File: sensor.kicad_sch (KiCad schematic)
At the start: 15 parts, among them IC1 A3909, J1 Micro_SD_Card_Det1, U2 IMU, U5 LPS22HB, U6 GPS, U7 SX1276, U8 NAND

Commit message: Changes, idr what though :(
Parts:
- removed R13: 10kΩ, symbol Device:R
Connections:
- net +3.3V: now also R12.1
- net GND: now also U7.15 (GND), U7.23 (GND), U7.26 (GND), U7.29 (GND)
- net MISO TMCU: now also U7.17 (MISO)
- net MOSI TMCU: now also U7.18 (MOSI)
- net at R12.2, U8.3 (~{WP}/IO_{2}): now also U8.7 (~{HOLD}/~{RESET}/IO_{3})
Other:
- note added: "Baro"
- note added: "Chip Selection"
- note added: "GPS"
- note added: "IMU"
- note added: "Interrupt Pin"
- note added: "RF"
- note added: "Storage/Logging"
- note added: "UART Lines"
- moved on the sheet: C14, C15, IC1, J1, R10, R12, R8, R9, U2, U5, U7, U8

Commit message: misc fixes
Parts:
- added C18: 4.7uF, symbol Device:C
- added C19: 100nF, symbol Device:C
- added D1: D_Schottky, symbol Device:D_Schottky
- added R19, R23: 10k, symbol Device:R
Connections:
- net +3.3V: now also C18.2, C19.2, D1.2 (A); no longer U6.8 (V_BCKP)
- net GND: now also C18.1, C19.1, R19.1, R23.1
- net at U7.8 (DIO0): now also R19.2
- net at U7.9 (DIO1): now also R23.2
- new net: D1.1 (K), U6.8 (V_BCKP)

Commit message: GPS is done! yay
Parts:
- added C20: 100nF, symbol Device:C
- added D2: PESD5V‑S5ULC, symbol Device:D
- added J3: Conn_Coaxial, symbol Connector:Conn_Coaxial
- added L1: 47 nH, Inductor_SMD:L_6.3x6.3_H3, symbol Device:L_Ferrite_Small
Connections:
- net +3.3V: now also L1.1
- net GND: now also D2.1 (K), J3.2 (Ext)
- net at U6.16 (RF_OUT): now also C20.2
- new net: C20.1, D2.2 (A), J3.1 (In), L1.2
- no-connect marks 7 -> 15
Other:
- note added: "Confirm L4 has ≥1 kΩ impedance at 1.575 GHz"
- note added: "No Noise within 3mm of this chain 50 Ω trace keep RF_OUT → C20 → SMA center < 5 mm"

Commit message: RF at 915MHZ done!
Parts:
- added C21: 2.2 pF, symbol Device:C
- added C22: 1.8 pF, symbol Device:C
- added J4: H9161TR-ND, symbol Connector:Conn_Coaxial_Small
- added L7: 5.6 nH, symbol Device:L
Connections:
- net GND: now also C22.1, J4.2 (Ext)
- net at U7.22 (RFO_HF): now also C21.1
- new net: C21.2, J4.1 (In), L7.1
- new net: C22.2, L7.2
- no-connect marks 15 -> 16
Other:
- note added: "No Noise within 3mm of this chain 50 Ω trace keep RF_OUT → C20 → SMA center < 6 mm"
- note added: "RF at 915MHZ"
- note removed: "RF"
- moved on the sheet: R19, R23, U7

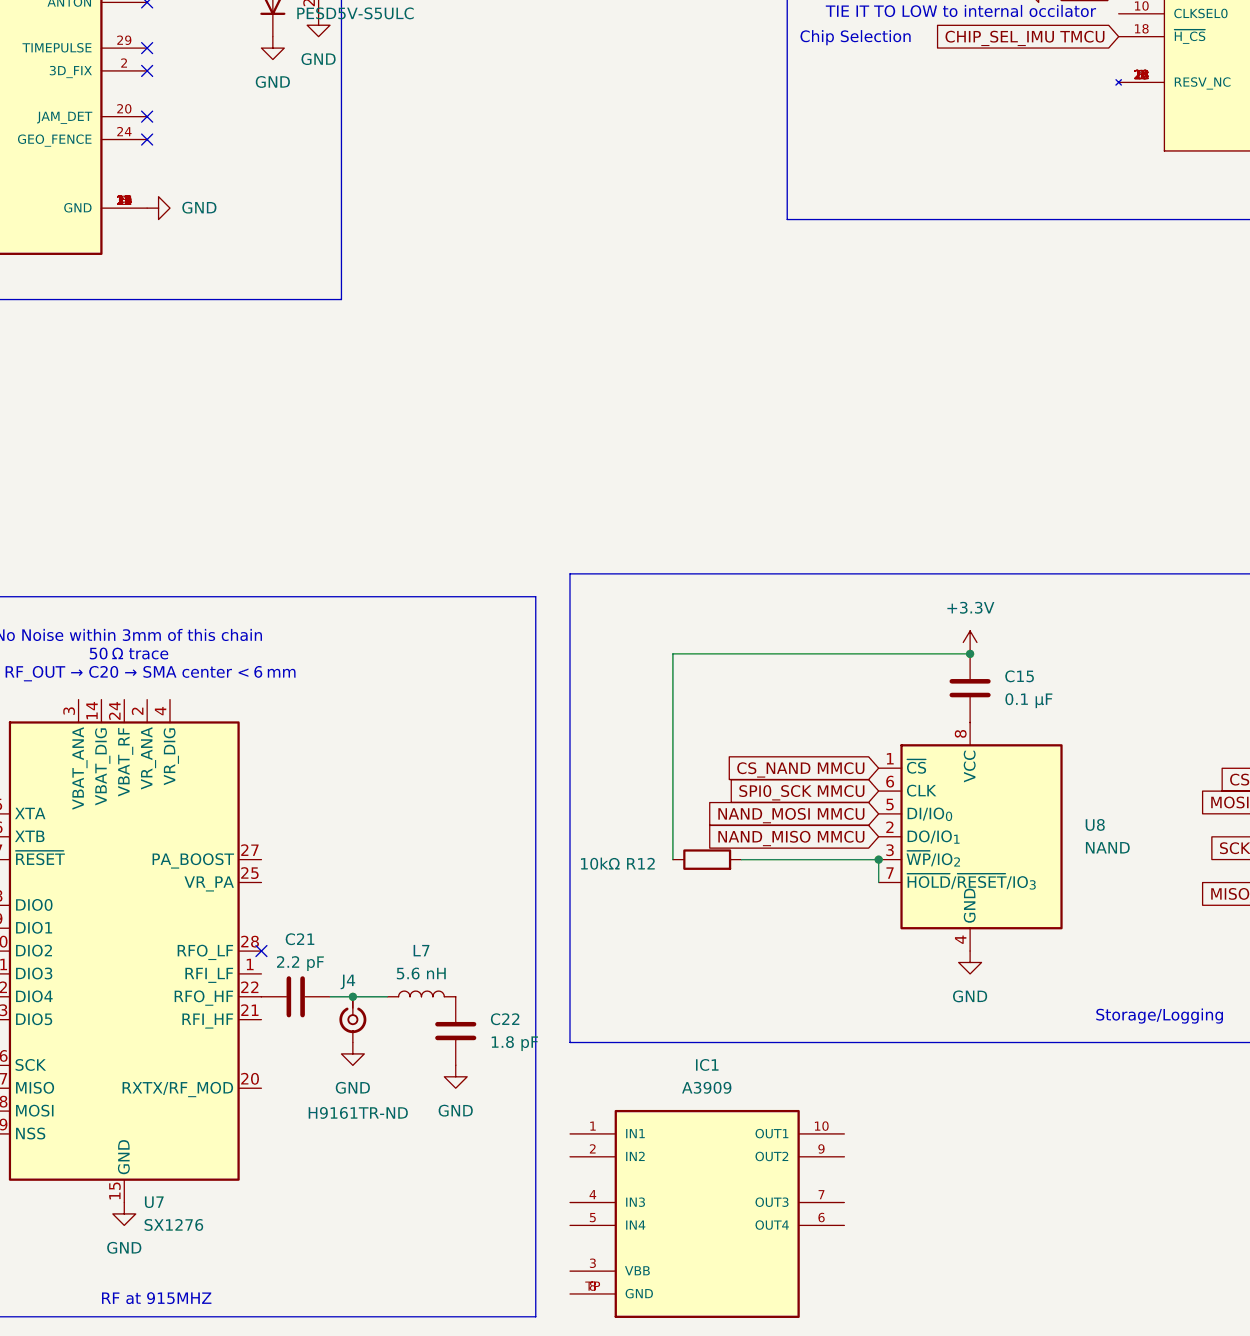
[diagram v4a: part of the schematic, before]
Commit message: H-Bridge is done!
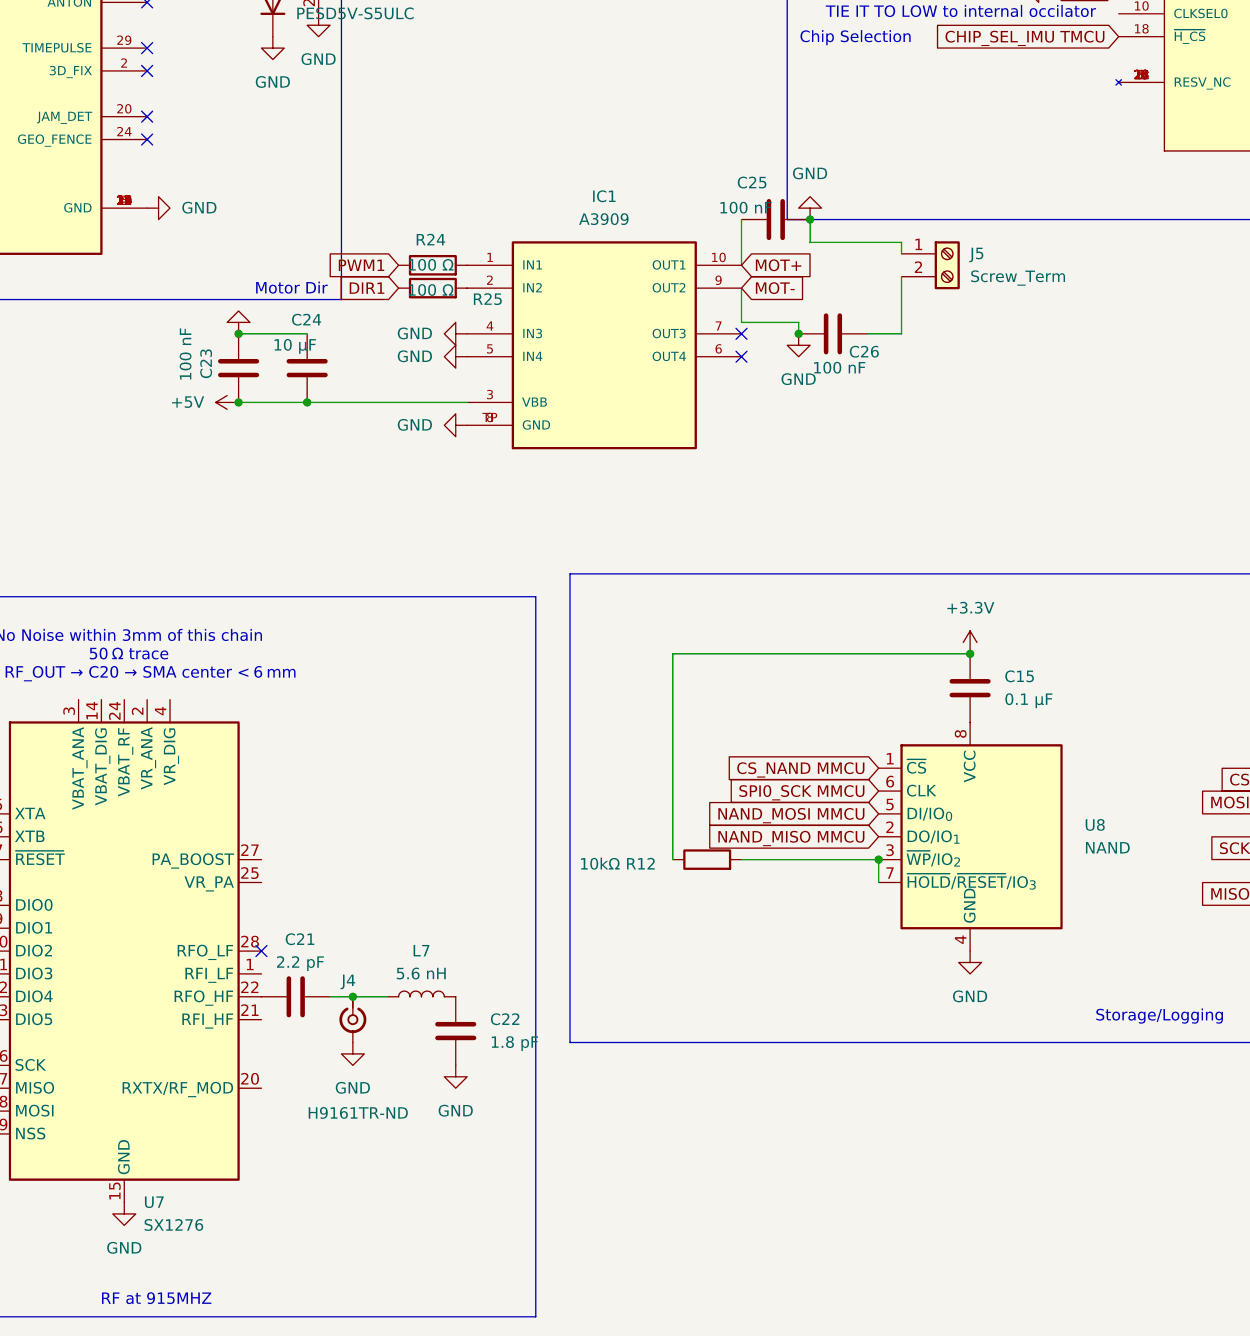
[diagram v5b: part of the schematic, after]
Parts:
- added C23, C25, C26: 100 nF, symbol Device:C
- added C24: 10 µF, symbol Device:C
- added J5: Screw_Term, symbol Connector:Screw_Terminal_01x02
- added R24, R25: 100 Ω, symbol Device:R
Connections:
- net GND: now also IC1.4 (IN3), IC1.5 (IN4), IC1.8 (GND), IC1.9 (OUT2), IC1.TP (GND), C23.1, C24.1, C25.1, C26.2, J5.1 (Pin_1)
- net at IC1.1 (IN1): now also R24.2
- net MOT+: now reaches IC1.10 (OUT1)
- net MOT+: now also C25.2
- net at IC1.2 (IN2): now also R25.2
- net +5V: now reaches IC1.3 (VBB)
- net +5V: now also C23.2, C24.2
- new net: C26.1, J5.2 (Pin_2)
- new net DIR1: R25.1
- new net PWM1: R24.1
- no-connect marks 16 -> 18
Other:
- note added: "Motor Dir"
- moved on the sheet: IC1

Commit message: Flag Changes- Important
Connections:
- net MISO_SD MMCU is gone; now on net NAND_MISO MMCU: J1.7 (DAT0)
- net MOSI_SD MMCU is gone; now on net NAND_MOSI MMCU: J1.3 (CMD)
- net SCK_SD MMCU renamed SPI0_SCK MMCU
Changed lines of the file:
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@@
 		)
 	)
-	(global_label "MOSI_SD MMCU"
+	(global_label "NAND_MOSI MMCU"
 		(shape input)
 		(at 227.33 138.43 180)
@@
 		)
 		(property "Intersheetrefs" "${INTERSHEET_REFS}"
-			(at 209.8306 138.43 0)
+			(at 207.2905 138.43 0)
 			(effects
 				(font
@@
 		)
 	)
-	(global_label "MISO_SD MMCU"
+	(global_label "NAND_MISO MMCU"
 		(shape input)
 		(at 227.33 148.59 180)
@@
 		)
 		(property "Intersheetrefs" "${INTERSHEET_REFS}"
-			(at 209.8306 148.59 0)
+			(at 207.2905 148.59 0)
 			(effects
 				(font
@@
 		)
 	)
-	(global_label "SCK_SD MMCU"
+	(global_label "SPI0_SCK MMCU"
 		(shape input)
 		(at 227.33 143.51 180)
@@
 		)
 		(property "Intersheetrefs" "${INTERSHEET_REFS}"
-			(at 210.6773 143.51 0)
-			(effects
-				(font
+			(at 208.863 143.51 0)
+			(effects
+				(font

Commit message: chip wiring fix
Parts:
- added C44, C45, C48, C49, C50, C51, C52, C53, C54, C55, C56, C57, C58: 100nF, symbol Device:C
- added C46, C47: 22pF, symbol Device:C_Polarized_US
- added J12, J13, J14, J6, J9: Conn_01x03, Connector_PinHeader_2.54mm:PinHeader_1x03_P2.54mm_Vertical, symbol Connector_Generic:Conn_01x03
- added Q1, Q3, Q4, Q5, Q6: 2N7002, Package_TO_SOT_SMD:SOT-23, symbol Transistor_FET:2N7002
- added R27, R31, R32, R33, R34, R35, R36, R37, R38, R39, R52, R53, R56, R57: 10k, symbol Device:R
- added R54, R55: 10kΩ, symbol Device:R
- added R58, R59, R60, R61, R62, R63, R64, R65, R66, R67: R, symbol Device:R
- added U10: LSM6DS3, Package_LGA:LGA-14_3x2.5mm_P0.5mm_LayoutBorder3x4y, symbol Sensor_Motion:LSM6DS3
- added Y2: 32.768kHz, symbol Device:Crystal
- C15: value 0.1 µF -> 100nF
- C24: value 10 µF -> 10nF
- C25: value 100 nF -> 100nF
- C26: value 100 nF -> 10nF
- R24, R25: value 100 Ω -> 10k
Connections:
- net +3.3V: now also U7.14 (VBAT_DIG), U7.2 (VR_ANA), U7.24 (VBAT_RF), U7.3 (VBAT_ANA), U7.4 (VR_DIG), U8.8 (VCC), C44.2, C45.2, C48.2, C49.2, C50.2, C51.2, C52.2, C53.2, C54.2, C55.2, C56.2, R27.1, R32.1, R33.1, R34.1, R35.1, R36.1, R37.1, R38.1, R39.1, R52.1, R53.1, R54.1, R55.1, R56.1, R57.1, U10.5 (VDDIO), U10.8 (VDD); no longer R11.1, R9.1
- net +5V: now also R58.1, R59.1, R60.1, R61.1, R62.1; no longer C24.2
- net CS_SD MMCU: now also R55.2
- net DIR1: now also IC1.2 (IN2), R24.2; no longer R25.1
- net GND: now also C15.2, C24.2, C25.2, R24.1, R25.1, R9.1, U2.10 (CLKSEL0), C44.1, C45.1, C46.2, C47.2, C48.1, C49.1, C50.1, C51.1, C52.1, C53.1, C54.1, C55.1, C56.1, C57.2, J12.3 (Pin_3), J13.3 (Pin_3), J14.3 (Pin_3), J6.3 (Pin_3), J9.3 (Pin_3), R31.1, U10.6 (GND), U10.7 (GND); no longer C24.1, C25.1, IC1.9 (OUT2), J5.1 (Pin_1)
- net INTERRUPT TMCU: now also R27.2, R36.2, U10.4 (INT1)
- net MISO TMCU: now also R33.2, R37.2, R53.2, U10.1 (SDO/SA0)
- net MOSI TMCU: now also R34.2, U10.2 (SDX)
- net PWM1: now also IC1.1 (IN1), R25.2; no longer R24.1
- net RESETN TMCU: now also R31.2
- net SPI_CLOCK TMCU: now also R32.2, U10.3 (SCX)
- net at U7.19 (NSS): now also R57.2
- net at U7.25 (VR_PA): now also C26.1, C57.1
- net at U7.27 (PA_BOOST): now also C24.1, C25.1
- net at R12.2, U8.3 (~{WP}/IO_{2}): no longer U8.7 (~{HOLD}/~{RESET}/IO_{3})
- net at U2.26 (XOUT32/CLKSEL1): now also C47.1, Y2.2
- net at U2.27 (XIN32): now also C46.1, Y2.1
- net SD_DETECT: now reaches J1.9 (DET)
- net SD_DETECT: now also R56.2
- net at J5.2 (Pin_2): now also IC1.9 (OUT2), C58.2; no longer C26.1
- net Baro_int TMCU: no longer names the net of U5.7 (INT_DRDY)
- net Baro_int TMCU: now also R52.2
- net CHIP_SEL TMCU renamed CS TMCU
- net CHIP_SEL_BARO TMCU renamed CS_BARO TMCU
- net CS_BARO TMCU: now also R39.2
- net CHIP_SEL_IMU TMCU renamed CS_IMU1
- net CS_IMU1: now also R35.2
- net MOT+: no longer names the net of IC1.10 (OUT1)
- net MOT+: now also J5.1 (Pin_1), C58.1; no longer C25.2
- new net: Q1.1 (G), R63.2
- new net: J14.2 (Pin_2), Q1.2 (S)
- new net: Q1.3 (D), R58.2
- new net: Q4.1 (G), R65.2
- new net: J6.2 (Pin_2), Q4.2 (S)
- new net: Q4.3 (D), R60.2
- new net: Q3.1 (G), R64.2
- new net: J13.2 (Pin_2), Q3.2 (S)
- new net: Q3.3 (D), R59.2
- new net: R54.2, U8.7 (~{HOLD}/~{RESET}/IO_{3})
- new net: Q6.3 (D), R62.2
- new net: Q5.1 (G), R66.2
- new net: Q6.1 (G), R67.2
- new net: Q5.3 (D), R61.2
- new net: J12.2 (Pin_2), Q6.2 (S)
- new net: J9.2 (Pin_2), Q5.2 (S)
- new net ANY GPIO PIN: R11.1
- new net CS_IMU TMCU: R38.2, U10.12 (CS)
- new net SERVO1: J14.1 (Pin_1)
- new net SERVO2: J13.1 (Pin_1)
- new net SERVO3: J6.1 (Pin_1)
- new net SERVO4: J9.1 (Pin_1)
- new net SERVO5: J12.1 (Pin_1)
- new net mosfet1_signal: R63.1
- new net mosfet2_signal: R64.1
- new net mosfet3_signal: R65.1
- new net mosfet4_signal: R66.1
- new net mosfet5_signal: R67.1
- no-connect marks 18 -> 13
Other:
- note removed: "Chip Selection"
- note removed: "Interrupt Pin"
- note removed: "TIE IT TO LOW to internal occilator"
- moved on the sheet: C15, C18, C23, IC1, J5, R12, R19, U5

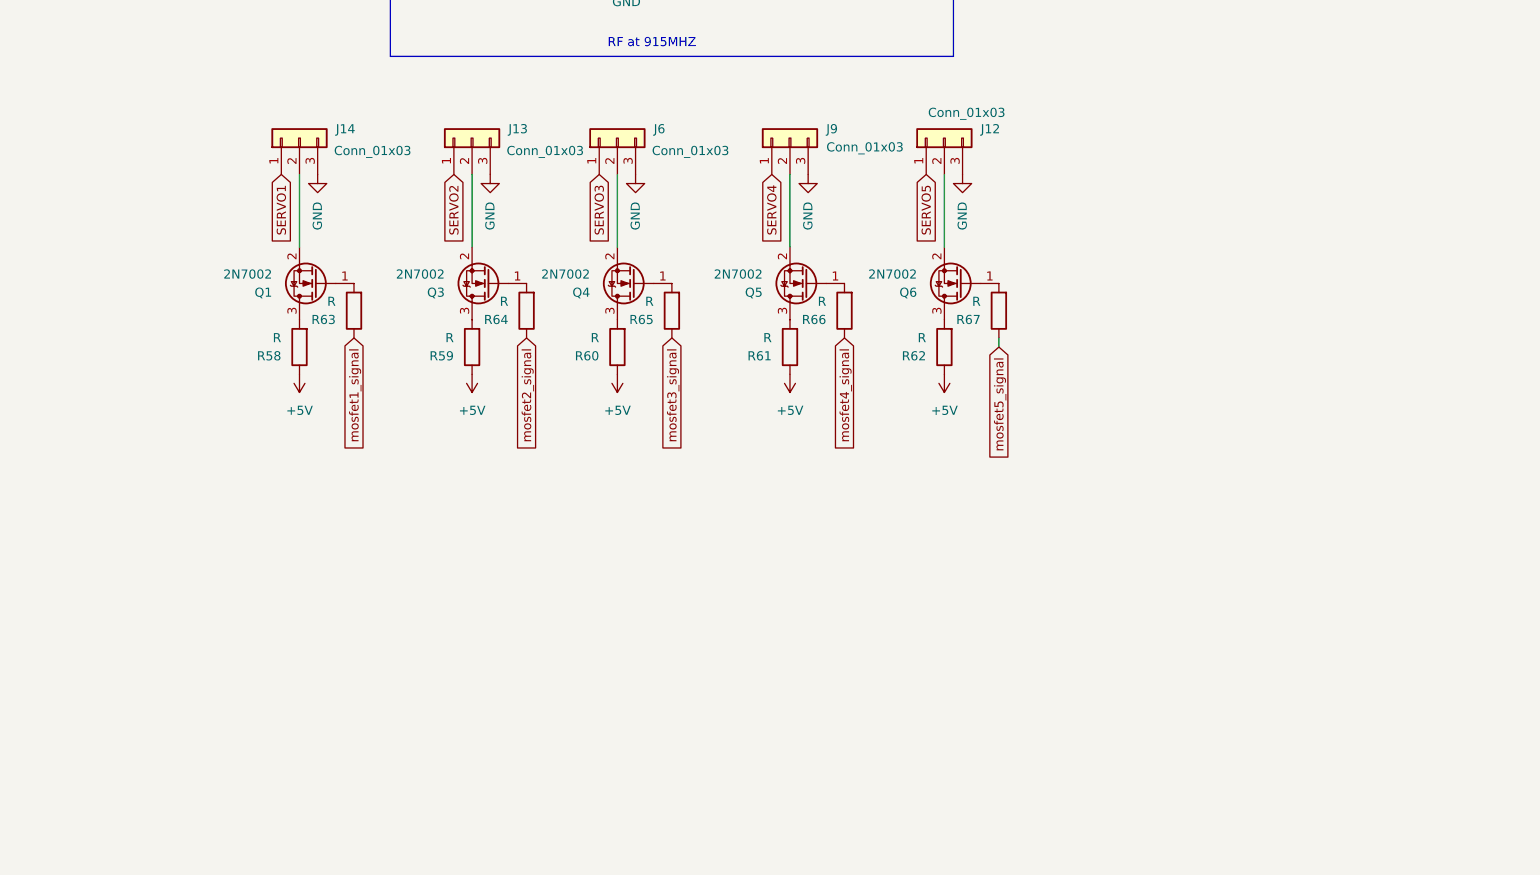
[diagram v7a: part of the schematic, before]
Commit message: servo mosfet, pyro mosfet, camera
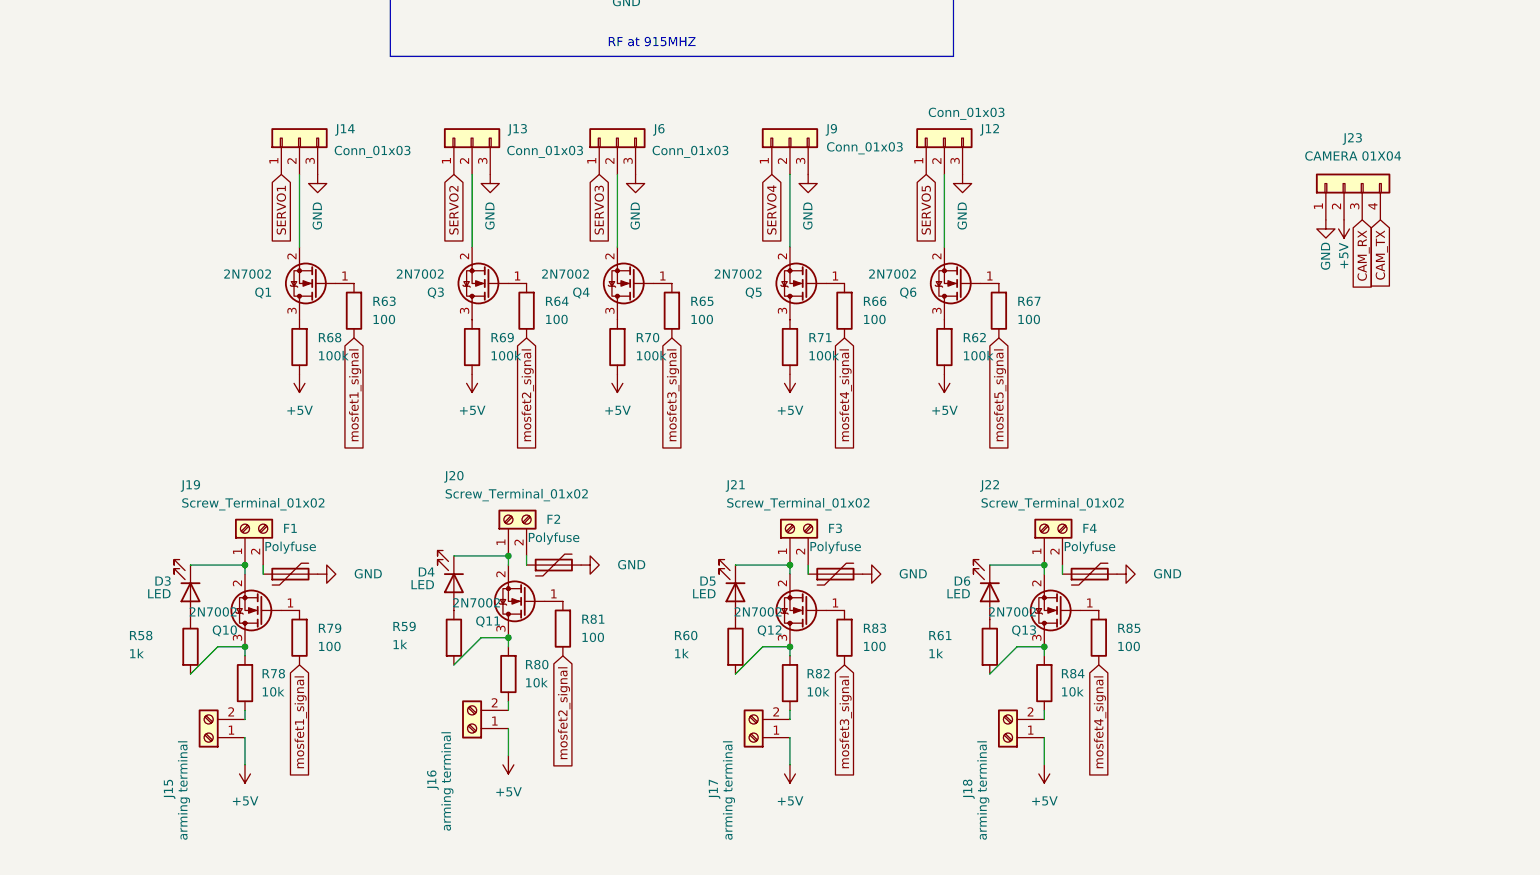
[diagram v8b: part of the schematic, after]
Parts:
- added D3, D4, D5, D6: LED, symbol Device:LED
- added F1, F2, F3, F4: Polyfuse, symbol Device:Polyfuse
- added J15, J16, J17, J18: arming terminal, symbol Connector:Screw_Terminal_01x02
- added J19, J20, J21, J22: Screw_Terminal_01x02, symbol Connector:Screw_Terminal_01x02
- added J23: CAMERA 01X04, symbol Connector_Generic:Conn_01x04
- added Q10, Q11, Q12, Q13: 2N7002, Package_TO_SOT_SMD:SOT-23, symbol Transistor_FET:2N7002
- added R68, R69, R70, R71: 100k, symbol Device:R
- added R78, R80, R82, R84: 10k, symbol Device:R
- added R79, R81, R83, R85: 100, symbol Device:R
- R58, R59, R60, R61: value R -> 1k
- R62: value R -> 100k
- R63, R64, R65, R66, R67: value R -> 100
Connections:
- net +5V: now also J15.1 (Pin_1), J16.1 (Pin_1), J17.1 (Pin_1), J18.1 (Pin_1), J23.2 (Pin_2), R68.1, R69.1, R70.1, R71.1; no longer R58.1, R59.1, R60.1, R61.1
- net GND: now also F1.2, F2.2, F3.2, F4.2, J23.1 (Pin_1)
- net mosfet1_signal: now also R79.1
- net mosfet2_signal: now also R81.1
- net mosfet3_signal: now also R83.1
- net mosfet4_signal: now also R85.1
- net at Q1.3 (D): now also R68.2; no longer R58.2
- net at Q4.3 (D): now also R70.2; no longer R60.2
- net at Q3.3 (D): now also R69.2; no longer R59.2
- net at R61.2: now also Q13.3 (D), R84.2; no longer Q5.3 (D)
- new net: Q12.1 (G), R83.2
- new net: D4.1 (K), J20.1 (Pin_1), Q11.2 (S)
- new net: D4.2 (A), R59.1
- new net: Q13.1 (G), R85.2
- new net: D6.1 (K), J22.1 (Pin_1), Q13.2 (S)
- new net: F2.1, J20.2 (Pin_2)
- new net: D5.1 (K), J21.1 (Pin_1), Q12.2 (S)
- new net: Q12.3 (D), R60.2, R82.2
- new net: D6.2 (A), R61.1
- new net: J16.2 (Pin_2), R80.1
- new net: Q11.3 (D), R59.2, R80.2
- new net: F3.1, J21.2 (Pin_2)
- new net: J18.2 (Pin_2), R84.1
- new net: Q10.1 (G), R79.2
- new net: Q5.3 (D), R71.2
- new net: D5.2 (A), R60.1
- new net: D3.1 (K), J19.1 (Pin_1), Q10.2 (S)
- new net: Q10.3 (D), R58.2, R78.2
- new net: J17.2 (Pin_2), R82.1
- new net: Q11.1 (G), R81.2
- new net: F4.1, J22.2 (Pin_2)
- new net: J15.2 (Pin_2), R78.1
- new net: D3.2 (A), R58.1
- new net: F1.1, J19.2 (Pin_2)
- new net CAM_RX: J23.3 (Pin_3)
- new net CAM_TX: J23.4 (Pin_4)
